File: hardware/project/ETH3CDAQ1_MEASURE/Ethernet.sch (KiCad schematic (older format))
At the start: 43 parts, among them U601 LAN8742A, U602 LC03-3.3, U603 LC03-3.3, Y601 NX5032GA-25.000M-LN-CD-1

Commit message: PCB layout
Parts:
- renumbered C601 to C401, C602 to C402, C603 to C403, C604 to C404, C605 to C405, C606 to C406, C607 to C407, C608 to C408, C609 to C409, C610 to C410, C611 to C411, C612 to C412, C613 to C413, C614 to C414, D601 to D401, D602 to D402, FB601 to FB401, L601 to L401, R601 to R401, R602 to R402, R603 to R403, R604 to R404, R605 to R405, R606 to R406, R607 to R407, R608 to R408, R609 to R409, R610 to R410, R611 to R411, R612 to R412, R613 to R413, R614 to R414, R615 to R415, R616 to R416, R617 to R417, R618 to R418, R619 to R419, R620 to R420, R621 to R421, U601 to U401, U602 to U402, U603 to U403, Y601 to Y401

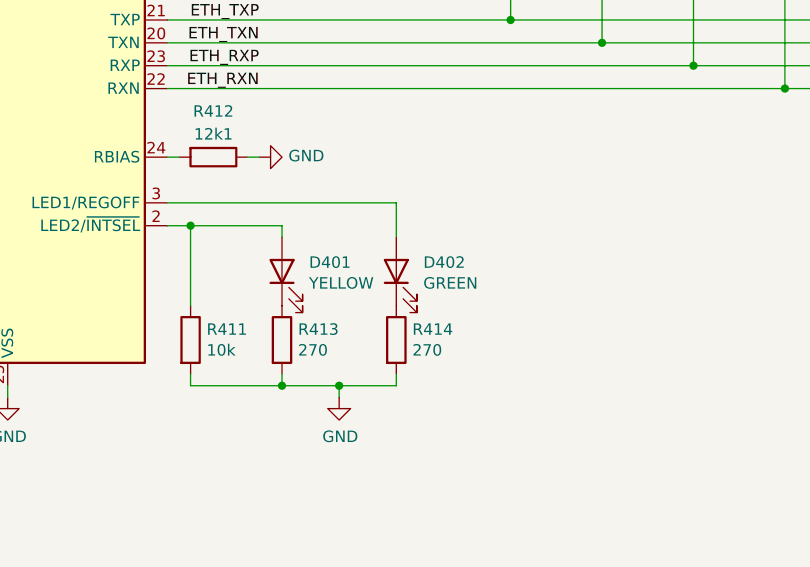
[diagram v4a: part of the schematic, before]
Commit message: SDRAM works, thanks to the website https://medium.com/@pjinwoo123/stm32h7-external-sdram-evaluation-board-cc72444898d8 . Modified the code to work with SDRAM BANK2. SCPI library works.
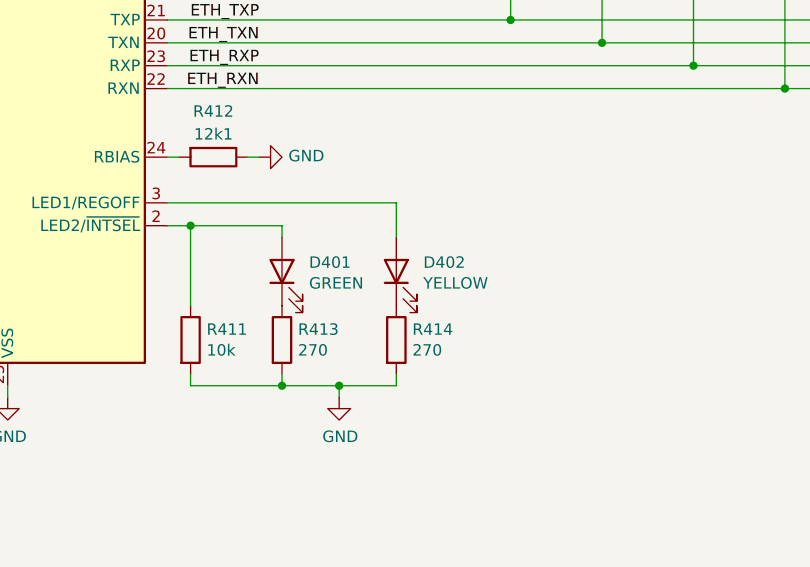
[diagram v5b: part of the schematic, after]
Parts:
- D401: value YELLOW -> GREEN
- D402: value GREEN -> YELLOW
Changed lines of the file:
@@
 P 4700 4000
 F 0 "D401" V 4739 3882 50  0000 R CNN
-F 1 "YELLOW" V 4648 3882 50  0000 R CNN
+F 1 "GREEN" V 4648 3882 50  0000 R CNN
 F 2 "LED_SMD:LED_0603_1608Metric_Pad1.05x0.95mm_HandSolder" H 4700 4000 50  0001 C CNN
 F 3 "~" H 4700 4000 50  0001 C CNN
@@
 P 5200 4000
 F 0 "D402" V 5239 3882 50  0000 R CNN
-F 1 "GREEN" V 5148 3882 50  0000 R CNN
+F 1 "YELLOW" V 5148 3882 50  0000 R CNN
 F 2 "LED_SMD:LED_0603_1608Metric_Pad1.05x0.95mm_HandSolder" H 5200 4000 50  0001 C CNN
 F 3 "~" H 5200 4000 50  0001 C CNN
